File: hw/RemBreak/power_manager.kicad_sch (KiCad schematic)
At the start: 17 parts, among them IC3 MAX17049G+T10, IC4 LTC2943IDD#TRPBF, J3 Screw_Terminal_01x02, J5 Conn_01x03, J6 Conn_01x02, U2 L7805, U3 INA219BxDCN, U7 L7805

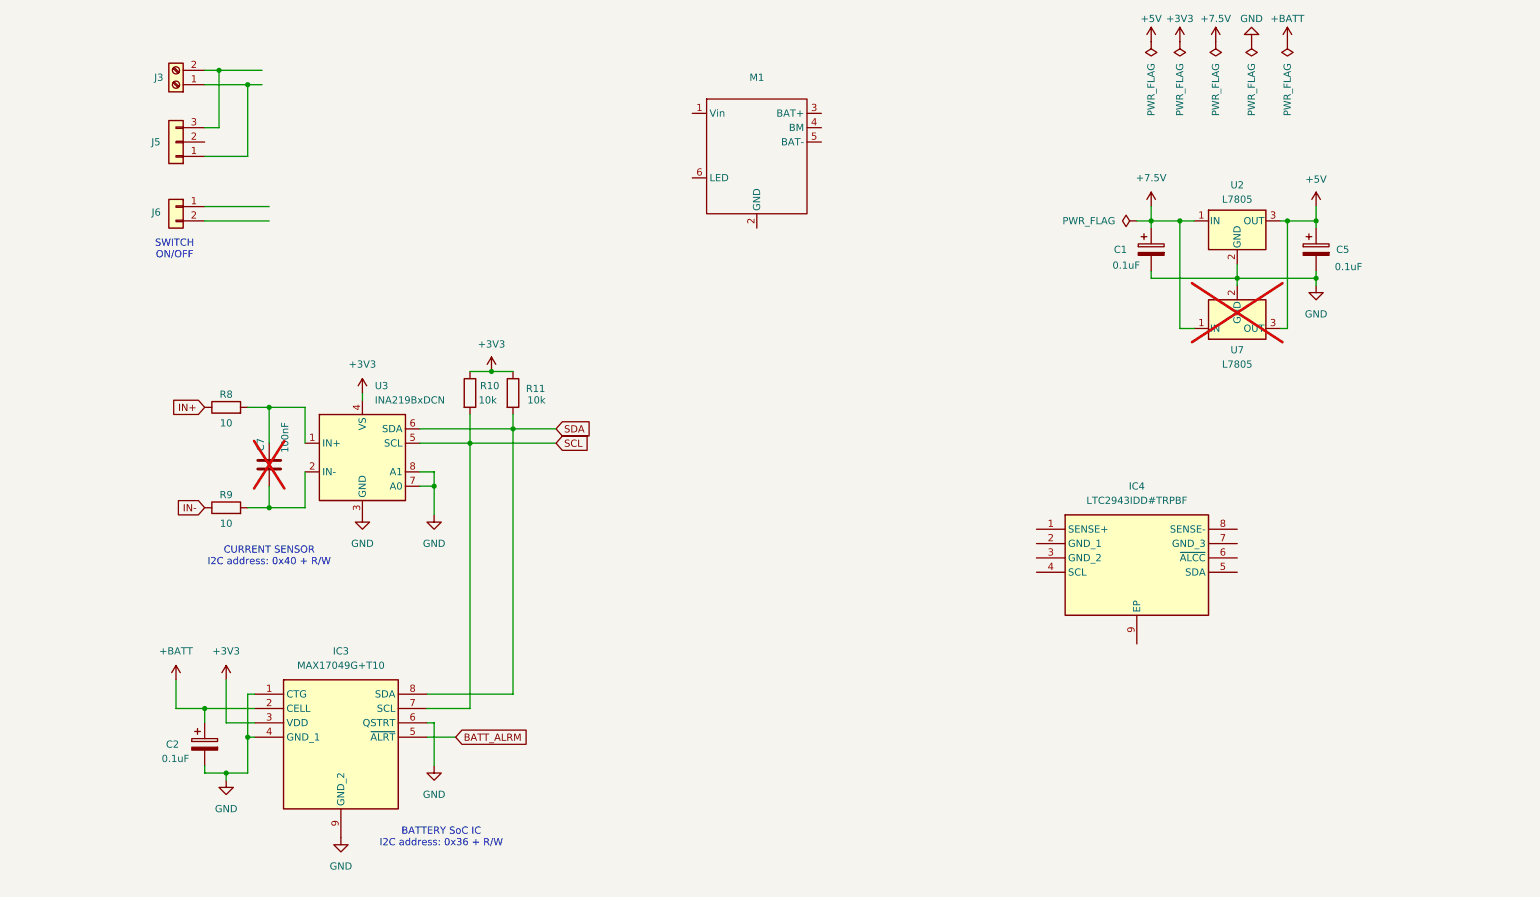
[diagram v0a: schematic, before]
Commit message: project update - started drawing the first revision of the board
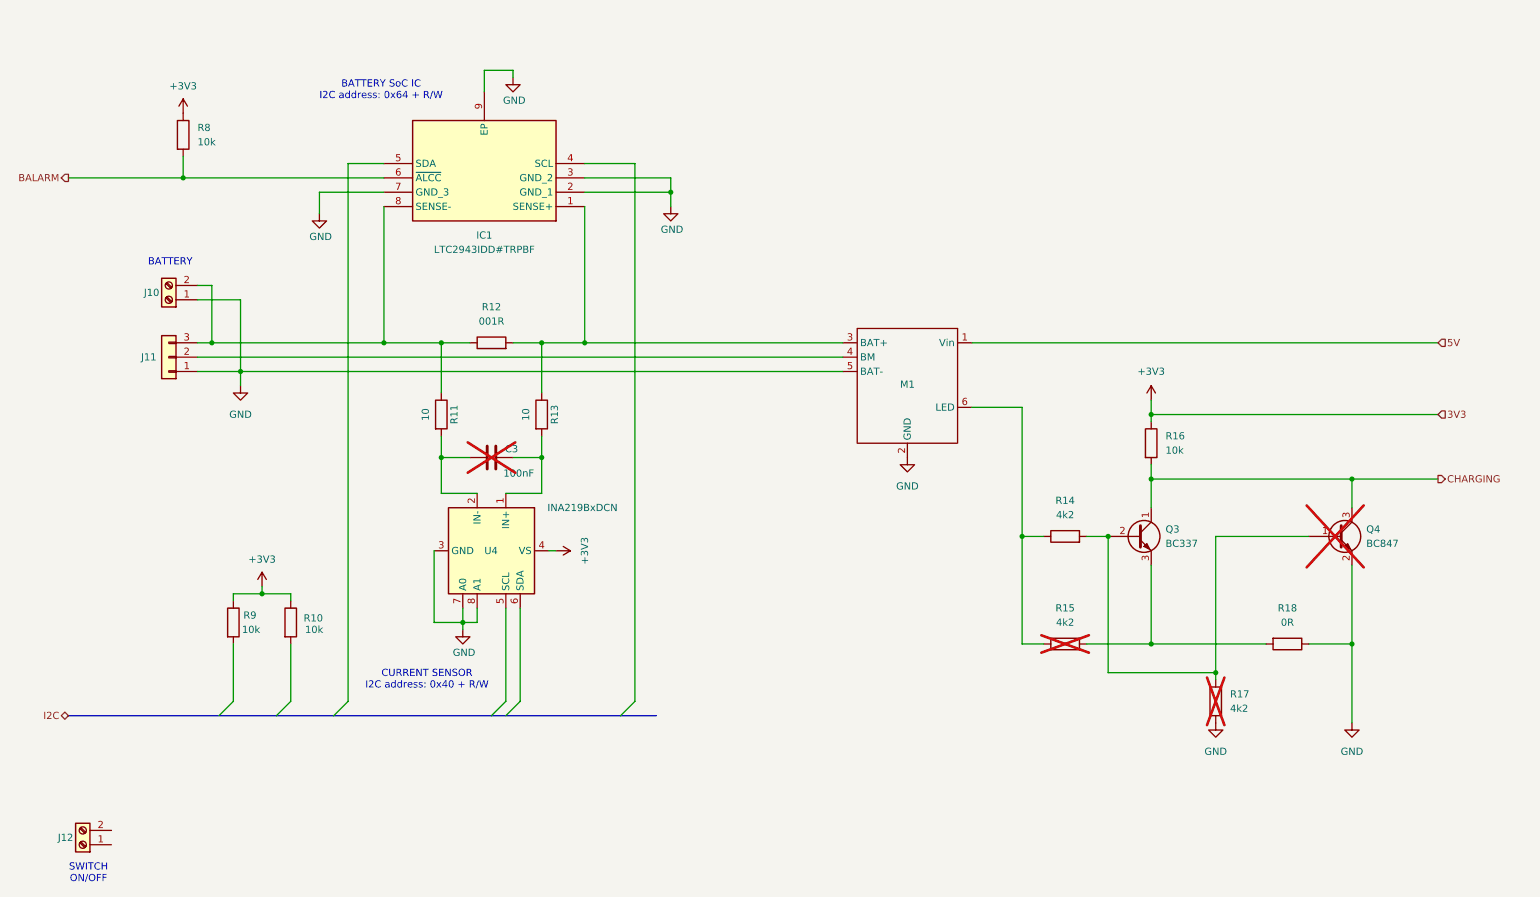
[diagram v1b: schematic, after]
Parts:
- removed C1, C2, C5: 0.1uF, symbol Device:C_Polarized
- removed IC3: MAX17049G+T10, Package_DFN_QFN:TDFN-8-1EP_2x2mm_P0.5mm_EP0.8x1.2mm, symbol dodo-power:MAX17049G+T10
- removed J6: Conn_01x02, symbol Connector_Generic:Conn_01x02
- removed U2, U7: L7805, symbol Regulator_Linear:L7805
- added J12: Screw_Terminal_01x02, TerminalBlock_Phoenix:TerminalBlock_Phoenix_MKDS-1,5-2_1x02_P5.00mm_Horizontal, symbol Connector:Screw_Terminal_01x02
- added Q3: BC337, Package_TO_SOT_THT:TO-92_Inline, symbol Transistor_BJT:BC337
- added Q4: BC847, Package_TO_SOT_SMD:SOT-23, symbol Transistor_BJT:BC847
- added R12: 001R, Resistor_SMD:R_2512_6332Metric_Pad1.40x3.35mm_HandSolder, symbol Device:R
- added R14, R15, R17: 4k2, Resistor_SMD:R_0805_2012Metric, symbol Device:R
- added R16, R8: 10k, Resistor_SMD:R_0805_2012Metric, symbol Device:R
- added R18: 0R, Resistor_SMD:R_0805_2012Metric, symbol Device:R
- C3: renamed from C7; footprint (none) -> Capacitor_SMD:C_0805_2012Metric
- IC1: renamed from IC4; footprint SON50P300X300X80-9N-D -> Package_DFN_QFN:DFN-8-1EP_3x3mm_P0.5mm_EP1.7x2.4mm
- J10: renamed from J3; footprint (none) -> TerminalBlock_Phoenix:TerminalBlock_Phoenix_MKDS-1,5-2_1x02_P5.00mm_Horizontal
- J11: renamed from J5; footprint (none) -> Connector_JST:JST_XH_B3B-XH-A_1x03_P2.50mm_Vertical
- M1: footprint (none) -> chinese_modules:USBC_charger
- R10: renamed from R11; footprint (none) -> Resistor_SMD:R_0805_2012Metric
- R11: renamed from R9; footprint (none) -> Resistor_SMD:R_0805_2012Metric
- R13: renamed from R8; footprint (none) -> Resistor_SMD:R_0805_2012Metric
- R9: renamed from R10; footprint (none) -> Resistor_SMD:R_0805_2012Metric
- renumbered U3 to U4
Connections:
- net IN+ is gone; now on an unnamed net: R13.1
- net IN- is gone; now on an unnamed net: R11.1
- net +3V3: now also R16.1, R8.1
- net GND: now also IC1.2 (GND_1), IC1.3 (GND_2), IC1.7 (GND_3), IC1.9 (EP), J10.1 (Pin_1), J11.1 (Pin_1), M1.2 (GND), M1.5 (BAT-), Q4.2 (E), R17.1, R18.1
- net at J10.2 (Pin_2), J11.3 (Pin_3): now also IC1.8 (SENSE-), R12.1
- net at IC1.1 (SENSE+): now also M1.3 (BAT+), R12.2
- net BALARM: now reaches IC1.6 (~{ALCC})
- net BALARM: now also R8.2
- net 5V: now reaches M1.1 (Vin)
- net at M1.4 (BM): now also J11.2 (Pin_2)
- net at M1.6 (LED): now also R14.1, R15.1
- net SCL: no longer names the net of U4.5 (SCL)
- net SCL: no longer R9.2
- net SDA: no longer names the net of R10.2
- net SDA: no longer U4.6 (SDA)
- new net: Q3.2 (B), Q4.1 (B), R14.2, R17.2
- new net: Q3.3 (E), R15.2, R18.2
- new net CHARGING: Q3.1 (C), Q4.3 (C), R16.2
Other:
- note added: "BATTERY"
- note added: "BATTERY SoC IC I2C address: 0x64 + R/W"
- note removed: "BATTERY SoC IC I2C address: 0x36 + R/W"
- moved on the sheet: C3, IC1, J10, J11, M1, R10, R11, R13, R9, U4

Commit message: schematics drawing in progress
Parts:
- removed J12: Screw_Terminal_01x02, TerminalBlock_Phoenix:TerminalBlock_Phoenix_MKDS-1,5-2_1x02_P5.00mm_Horizontal, symbol Connector:Screw_Terminal_01x02
- added U7: MAX40200AUK, Package_TO_SOT_SMD:SOT-23-5, symbol Analog_Switch:MAX40200AUK
- renumbered C3 to C4, Q3 to Q4, Q4 to Q5, R9 to R12, R10 to R13, R11 to R14, R12 to R15, R13 to R16, R14 to R17, R15 to R18, R16 to R19, R17 to R20, R18 to R21, R8 to R22, U4 to U6
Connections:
- net GND: now also U7.2 (GND)
- net VBATT: now reaches IC1.1 (SENSE+), M1.3 (BAT+), R15.2, R16.1
- net 5V: no longer names the net of M1.1 (Vin)
- net 5V: now also U7.5 (OUT)
- new net EN: U7.3 (EN)
- new net VBUS: U7.1 (VDD)
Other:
- note removed: "SWITCH ON/OFF"
- moved on the sheet: C4, IC1, M1, Q4, Q5, R12, R13, R14, R15, R16, R17, R18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

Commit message: changes in power line sharing in progress
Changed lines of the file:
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@@
 	(wire
 		(pts
-			(xy 252.73 49.53) (xy 133.35 49.53)
+			(xy 252.73 45.72) (xy 133.35 45.72)
 		)
 		(stroke
@@
 	(wire
 		(pts
-			(xy 133.35 49.53) (xy 133.35 58.42)
+			(xy 133.35 45.72) (xy 133.35 58.42)
 		)
 		(stroke
@@
 	(hierarchical_label "VBATT"
 		(shape output)
-		(at 252.73 49.53 0)
+		(at 252.73 45.72 0)
 		(fields_autoplaced yes)
 		(effects

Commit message: updated pcb and schematics - still in progress
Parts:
- J11: footprint Connector_JST:JST_XH_B3B-XH-A_1x03_P2.50mm_Vertical -> Connector_JST:JST_XH_S3B-XH-SM4-TB_1x03-1MP_P2.50mm_Horizontal
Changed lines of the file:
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@@
 			)
 		)
-		(property "Footprint" "Connector_JST:JST_XH_B3B-XH-A_1x03_P2.50mm_Vertical"
+		(property "Footprint" "Connector_JST:JST_XH_S3B-XH-SM4-TB_1x03-1MP_P2.50mm_Horizontal"
 			(at 34.29 90.17 0)
 			(effects

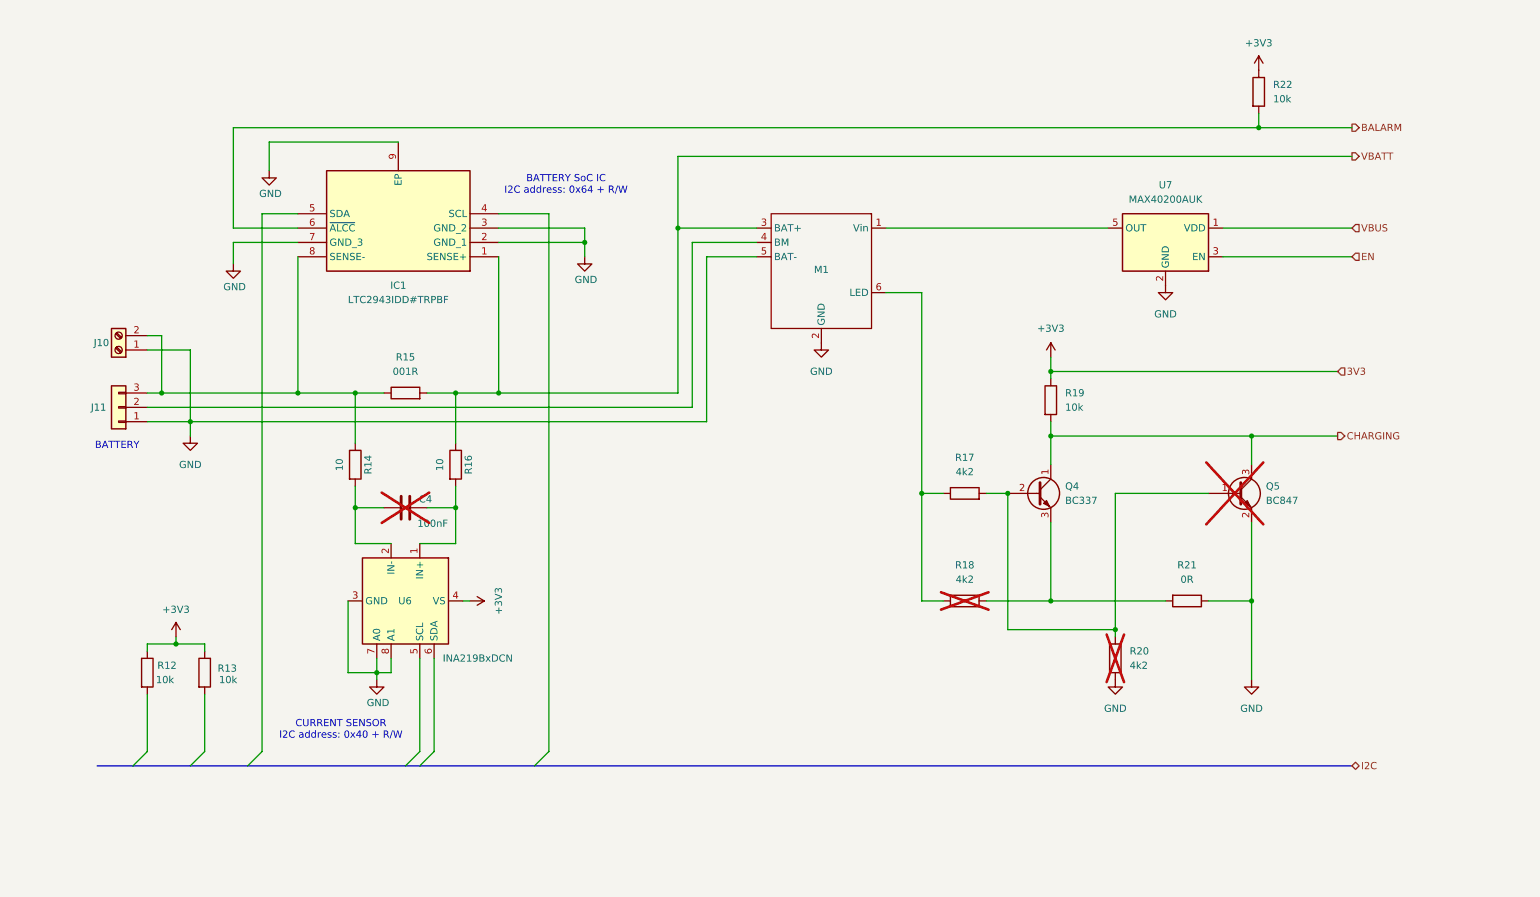
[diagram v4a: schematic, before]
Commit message: added RGB LED connection - missing connections in schematics
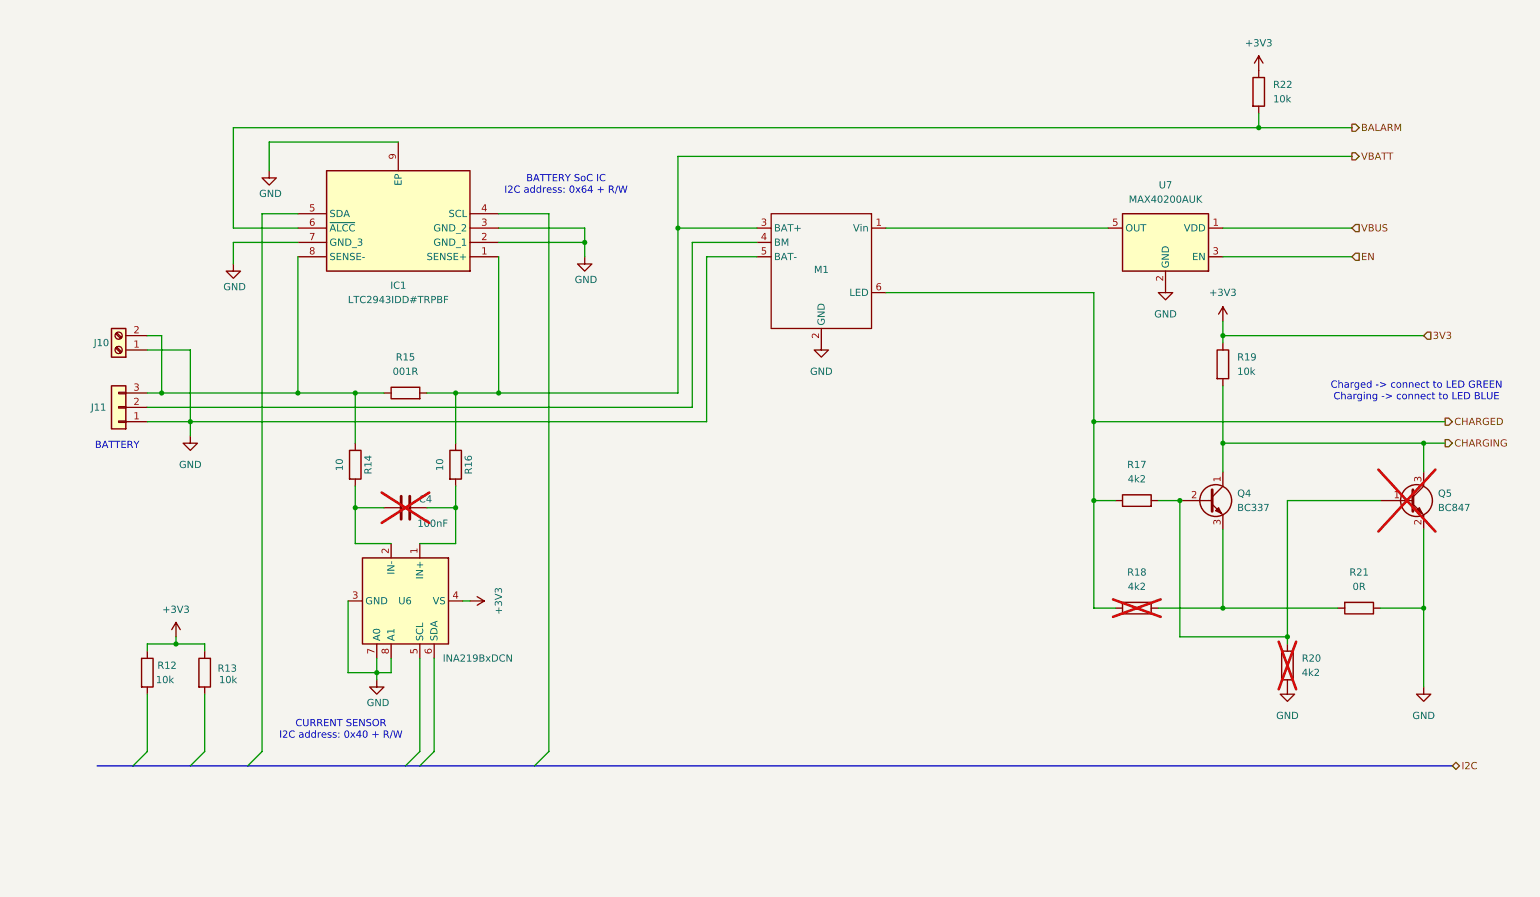
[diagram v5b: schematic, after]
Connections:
- net CHARGED: now reaches M1.6 (LED), R17.1, R18.1
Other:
- note added: "Charged -> connect to LED GREEN Charging -> connect to LED BLUE"
- moved on the sheet: Q4, Q5, R17, R18, R19, R20, R21

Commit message: finished schematics routing and erc passed
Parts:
- removed U6: INA219BxDCN, Package_TO_SOT_SMD:SOT-23-8, symbol Analog_ADC:INA219BxDCN
- added U5: INA219BxDCN, Package_TO_SOT_SMD:SOT-23-8, symbol Sensor_Energy:INA219BxDCN
- IC1: footprint Package_DFN_QFN:DFN-8-1EP_3x3mm_P0.5mm_EP1.7x2.4mm -> Package_DFN_QFN:DFN-8-1EP_3x3mm_P0.5mm_EP1.66x2.38mm
- M1: footprint chinese_modules:USBC_charger -> (none)
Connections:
- net +3V3: now also U5.4 (VS)
- net GND: now also U5.3 (GND), U5.7 (A0), U5.8 (A1)
- net I2C.SCL: now reaches R13.2
- net I2C.SCL: now also IC1.4 (SCL), U5.5 (SCL)
- net I2C.SDA: now reaches IC1.5 (SDA)
- net I2C.SDA: now also R12.2, U5.6 (SDA)
- net at C4.1, R14.2: now also U5.2 (IN-)
- net at C4.2, R16.2: now also U5.1 (IN+)
- net CHARGED renamed CHARGED (GREEN)
- net CHARGING renamed CHARGING (BLUE)
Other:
- moved on the sheet: J10, J11, Q4, Q5, R12, R13, R17, R18, R19, R20, R21, R22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

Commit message: fixed errors in schematics
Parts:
- M1: footprint (none) -> chinese_modules:USBC_charger
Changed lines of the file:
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@@
 			)
 		)
-		(property "Footprint" ""
+		(property "Footprint" "chinese_modules:USBC_charger"
 			(at 167.64 72.39 0)
 			(effects
